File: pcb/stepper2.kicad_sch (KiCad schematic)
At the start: 49 parts, among them J1 DA15_Receptacle_MountingHoles, J10 Conn_01x07_Pin, J2 DA15_Receptacle_MountingHoles, J3 DA15_Receptacle_MountingHoles, J4 DE15_Receptacle_HighDensity, J5 DE15_Receptacle_HighDensity, J6 DE15_Receptacle_HighDensity, J7 Conn_01x04_Pin, J8 Conn_01x05_Pin, J9 Conn_01x06_Pin, SW1 SW_Push, U1 AM26LS32ACN, U2 AM26LS32Ax, U3 AM26LS32ACN, U4 TMC2209_BIGTREETECH, U5 TMC2209_BIGTREETECH, U6 TMC2209_BIGTREETECH

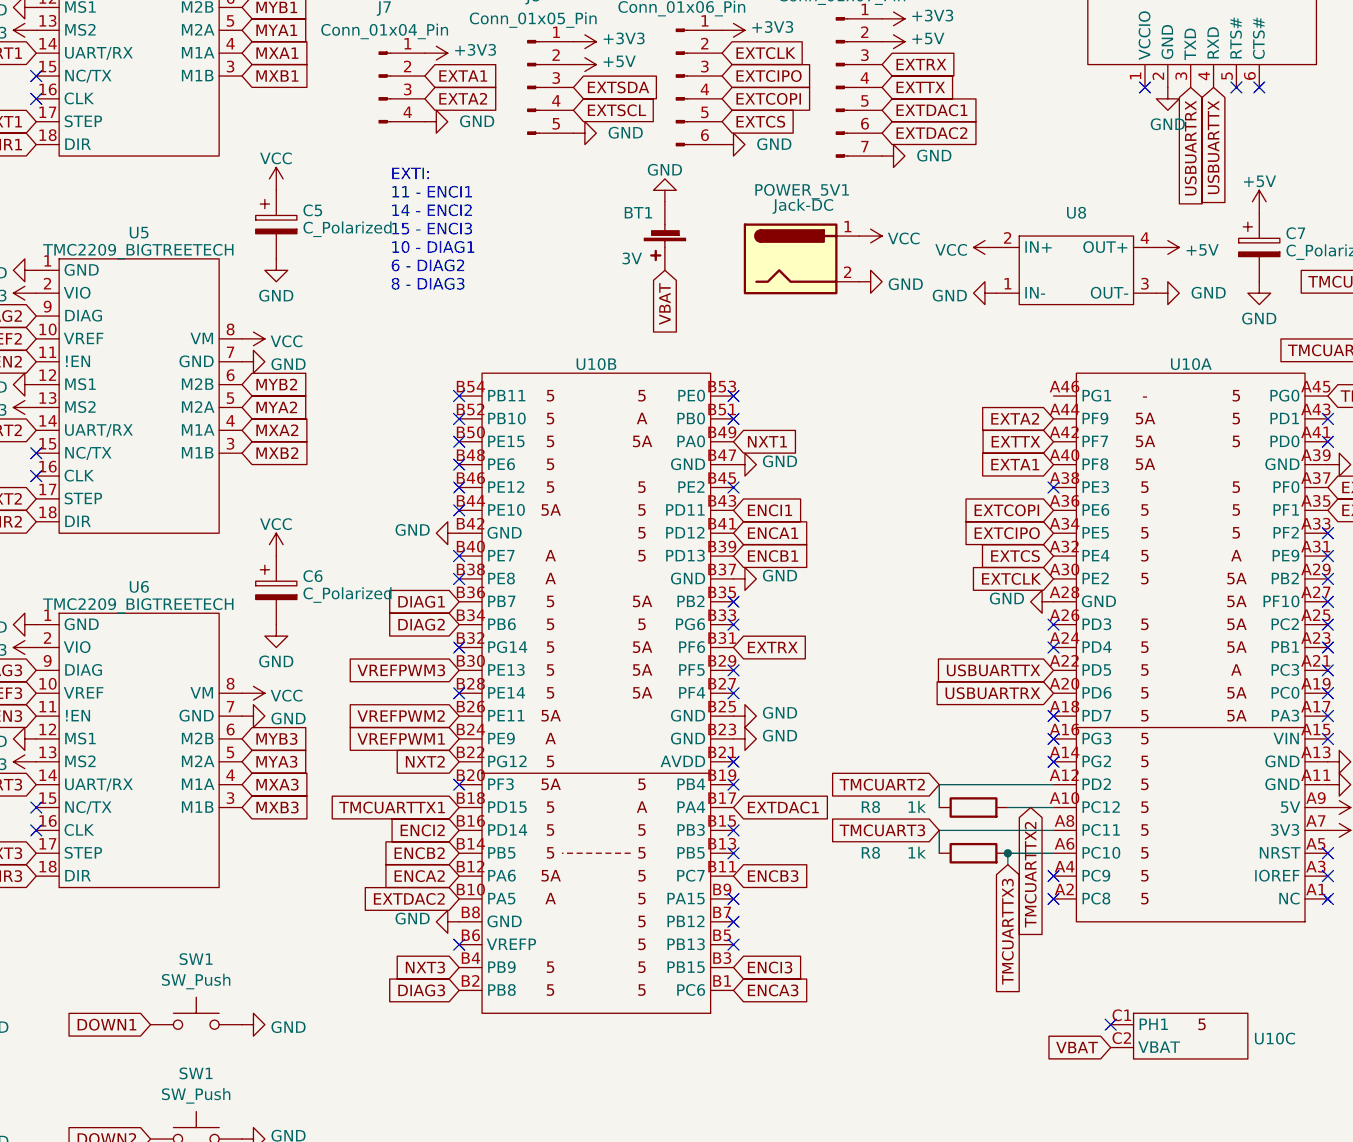
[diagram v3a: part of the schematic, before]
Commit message: Added missing limit switch GPIO and button gpio
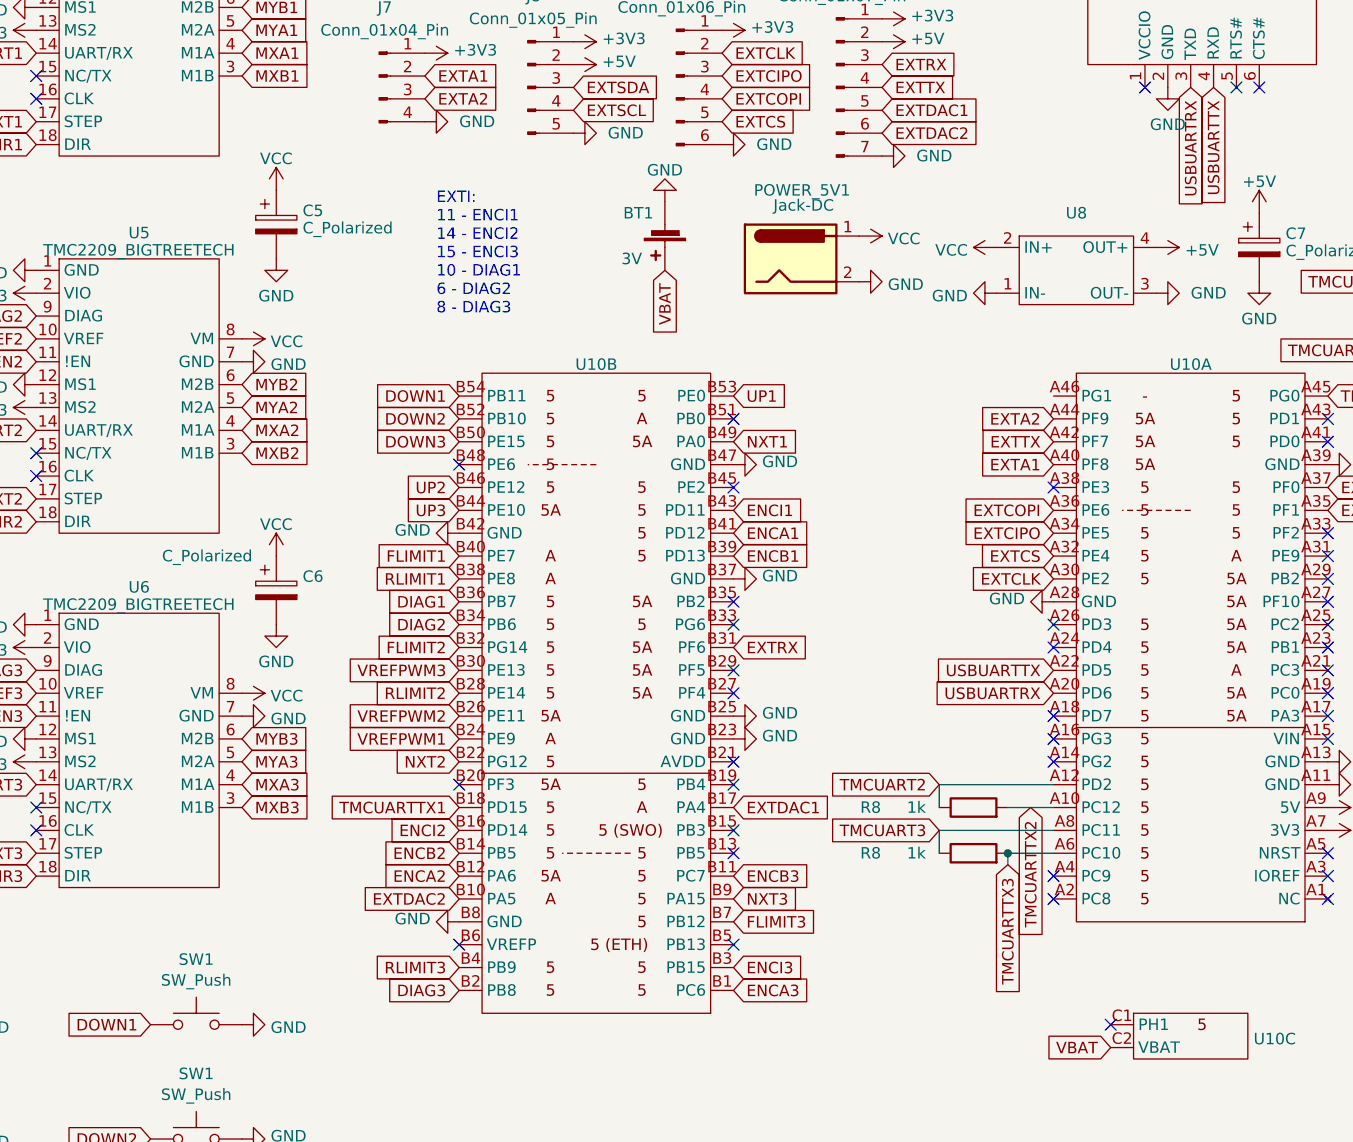
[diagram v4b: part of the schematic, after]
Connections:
- net DOWN1: now also U10.B54 (PB11)
- net DOWN2: now also U10.B52 (PB10)
- net DOWN3: now also U10.B50 (PE15)
- net FLIMIT1: now also U10.B40 (PE7)
- net FLIMIT2: now also U10.B32 (PG14)
- net FLIMIT3: now also U10.B7 (PB12)
- net NXT3: now also U10.B9 (PA15); no longer U10.B4 (PB9)
- net RLIMIT1: now also U10.B38 (PE8)
- net RLIMIT2: now also U10.B28 (PE14)
- net RLIMIT3: now also U10.B4 (PB9)
- net UP1: now also U10.B53 (PE0)
- net UP2: now also U10.B46 (PE12)
- net UP3: now also U10.B44 (PE10)
- no-connect marks 109 -> 97
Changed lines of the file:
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@@
   (no_connect (at 271.78 137.16))
   (no_connect (at 271.78 124.46))
-  (no_connect (at 175.26 88.9))
   (no_connect (at 247.65 156.21))
-  (no_connect (at 175.26 91.44))
-  (no_connect (at 175.26 114.3))
   (no_connect (at 80.01 184.15))
   (no_connect (at 128.27 53.34))
@@
   (no_connect (at 205.74 109.22))
   (no_connect (at 21.59 100.33))
-  (no_connect (at 205.74 137.16))
   (no_connect (at 21.59 33.02))
-  (no_connect (at 205.74 142.24))
   (no_connect (at 271.78 121.92))
   (no_connect (at 270.51 33.02))
   (no_connect (at 128.27 95.25))
-  (no_connect (at 205.74 144.78))
   (no_connect (at 205.74 116.84))
+  (no_connect (at 205.74 129.54))
   (no_connect (at 21.59 147.32))
-  (no_connect (at 205.74 134.62))
+  (no_connect (at 205.74 137.16))
   (no_connect (at 97.79 85.09))
   (no_connect (at 271.78 111.76))
@@
   (no_connect (at 113.03 77.47))
   (no_connect (at 113.03 92.71))
-  (no_connect (at 175.26 99.06))
-  (no_connect (at 175.26 104.14))
   (no_connect (at 241.3 96.52))
   (no_connect (at 21.59 102.87))
+  (no_connect (at 175.26 93.98))
   (no_connect (at 271.78 104.14))
   (no_connect (at 175.26 147.32))
@@
   (no_connect (at 271.78 142.24))
   (no_connect (at 128.27 92.71))
-  (no_connect (at 205.74 86.36))
   (no_connect (at 270.51 30.48))
   (no_connect (at 242.57 30.48))
@@
   (no_connect (at 270.51 38.1))
   (no_connect (at 97.79 58.42))
-  (no_connect (at 175.26 106.68))
   (no_connect (at 241.3 124.46))
   (no_connect (at 271.78 119.38))
@@
   (no_connect (at 270.51 40.64))
   (no_connect (at 97.79 95.25))
-  (no_connect (at 175.26 86.36))
-  (no_connect (at 205.74 147.32))
   (no_connect (at 113.03 55.88))
   (no_connect (at 113.03 116.84))
@@
   (no_connect (at 205.74 96.52))
   (no_connect (at 242.57 33.02))
+  (no_connect (at 205.74 147.32))
   (no_connect (at 271.78 101.6))
   (no_connect (at 21.59 95.25))
@@
   (no_connect (at 241.3 139.7))
   (no_connect (at 205.74 119.38))
-  (no_connect (at 205.74 129.54))
+  (no_connect (at 205.74 134.62))
   (no_connect (at 241.3 111.76))
   (no_connect (at 242.57 35.56))
   (no_connect (at 241.3 127))
-  (no_connect (at 175.26 119.38))
   (no_connect (at 21.59 40.64))
   (no_connect (at 21.59 154.94))
-  (no_connect (at 175.26 93.98))
   (no_connect (at 242.57 40.64))
   (no_connect (at 113.03 132.08))
   (no_connect (at 97.79 124.46))
-  (no_connect (at 175.26 96.52))
   (wire (pts (xy 36.83 45.72) (xy 36.83 48.26))
     (stroke (width 0) (type default))
@@
   )
   (text "EXTI:\n11 - ENCI1\n14 - ENCI2\n15 - ENCI3\n10 - DIAG1\n6 - DIAG2\n8 - DIAG3\n"
-    (at 167.64 74.93 0)
+    (at 172.72 77.47 0)
     (effects (font (size 1.27 1.27)) (justify left bottom))
   )
@@
     )
   )
+  (global_label "UP2" (shape input) (at 175.26 96.52 180) (fields_autoplaced)
+    (effects (font (size 1.27 1.27)) (justify right))
+    (property "Intersheetrefs" "${INTERSHEET_REFS}" (at 168.5442 96.52 0)
+      (effects (font (size 1.27 1.27)) (justify right) hide)
+    )
+  )
   (global_label "EN2" (shape input) (at 128.27 82.55 180) (fields_autoplaced)
     (effects (font (size 1.27 1.27)) (justify right))
@@
     )
   )
+  (global_label "DOWN3" (shape input) (at 175.26 91.44 180) (fields_autoplaced)
+    (effects (font (size 1.27 1.27)) (justify right))
+    (property "Intersheetrefs" "${INTERSHEET_REFS}" (at 165.7623 91.44 0)
+      (effects (font (size 1.27 1.27)) (justify right) hide)
+    )
+  )
   (global_label "ENCA2+" (shape input) (at 21.59 113.03 180) (fields_autoplaced)
     (effects (font (size 1.27 1.27)) (justify right))
@@
     )
   )
+  (global_label "RLIMIT2" (shape input) (at 175.26 119.38 180)
+    (effects (font (size 1.27 1.27)) (justify right))
+    (property "Intersheetrefs" "${INTERSHEET_REFS}" (at 175.26 119.38 0)
+      (effects (font (size 1.27 1.27)) hide)
+    )
+  )
   (global_label "ENCI1+" (shape input) (at 50.8 49.53 180) (fields_autoplaced)
     (effects (font (size 1.27 1.27)) (justify right))
@@
     )
   )
+  (global_label "DOWN2" (shape input) (at 175.26 88.9 180) (fields_autoplaced)
+    (effects (font (size 1.27 1.27)) (justify right))
+    (property "Intersheetrefs" "${INTERSHEET_REFS}" (at 165.7623 88.9 0)
+      (effects (font (size 1.27 1.27)) (justify right) hide)
+    )
+  )
   (global_label "EXTDAC2" (shape input) (at 175.26 142.24 180) (fields_autoplaced)
     (effects (font (size 1.27 1.27)) (justify right))
@@
     )
   )
+  (global_label "UP3" (shape input) (at 175.26 99.06 180) (fields_autoplaced)
+    (effects (font (size 1.27 1.27)) (justify right))
+    (property "Intersheetrefs" "${INTERSHEET_REFS}" (at 168.5442 99.06 0)
+      (effects (font (size 1.27 1.27)) (justify right) hide)
+    )
+  )
   (global_label "ENCB3" (shape input) (at 80.01 156.21 0) (fields_autoplaced)
     (effects (font (size 1.27 1.27)) (justify left))
@@
     )
   )
+  (global_label "FLIMIT2" (shape input) (at 175.26 114.3 180)
+    (effects (font (size 1.27 1.27)) (justify right))
+    (property "Intersheetrefs" "${INTERSHEET_REFS}" (at 175.26 114.3 0)
+      (effects (font (size 1.27 1.27)) hide)
+    )
+  )
   (global_label "ENCI2-" (shape input) (at 36.83 113.03 0) (fields_autoplaced)
     (effects (font (size 1.27 1.27)) (justify left))
@@
     )
   )
+  (global_label "RLIMIT3" (shape input) (at 175.26 149.86 180)
+    (effects (font (size 1.27 1.27)) (justify right))
+    (property "Intersheetrefs" "${INTERSHEET_REFS}" (at 175.26 149.86 0)
+      (effects (font (size 1.27 1.27)) hide)
+    )
+  )
   (global_label "VREF3" (shape input) (at 128.27 119.38 180)
     (effects (font (size 1.27 1.27)) (justify right))
@@
     )
   )
+  (global_label "DOWN1" (shape input) (at 175.26 86.36 180) (fields_autoplaced)
+    (effects (font (size 1.27 1.27)) (justify right))
+    (property "Intersheetrefs" "${INTERSHEET_REFS}" (at 165.7623 86.36 0)
+      (effects (font (size 1.27 1.27)) (justify right) hide)
+    )
+  )
   (global_label "ENCA2-" (shape input) (at 50.8 86.36 180) (fields_autoplaced)
     (effects (font (size 1.27 1.27)) (justify right))
@@
     )
   )
+  (global_label "RLIMIT1" (shape input) (at 175.26 106.68 180)
+    (effects (font (size 1.27 1.27)) (justify right))
+    (property "Intersheetrefs" "${INTERSHEET_REFS}" (at 175.26 106.68 0)
+      (effects (font (size 1.27 1.27)) hide)
+    )
+  )
   (global_label "MXB3" (shape input) (at 151.13 132.08 0) (fields_autoplaced)
     (effects (font (size 1.27 1.27)) (justify left))
@@
     )
   )
+  (global_label "UP1" (shape input) (at 205.74 86.36 0) (fields_autoplaced)
+    (effects (font (size 1.27 1.27)) (justify left))
+    (property "Intersheetrefs" "${INTERSHEET_REFS}" (at 212.4558 86.36 0)
+      (effects (font (size 1.27 1.27)) (justify left) hide)
+    )
+  )
   (global_label "MYA2" (shape input) (at 97.79 92.71 180) (fields_autoplaced)
     (effects (font (size 1.27 1.27)) (justify right))
@@
     )
   )
-  (global_label "NXT3" (shape input) (at 175.26 149.86 180) (fields_autoplaced)
-    (effects (font (size 1.27 1.27)) (justify right))
-    (property "Intersheetrefs" "${INTERSHEET_REFS}" (at 167.6371 149.86 0)
-      (effects (font (size 1.27 1.27)) (justify right) hide)
+  (global_label "NXT3" (shape input) (at 205.74 142.24 0) (fields_autoplaced)
+    (effects (font (size 1.27 1.27)) (justify left))
+    (property "Intersheetrefs" "${INTERSHEET_REFS}" (at 213.3629 142.24 0)
+      (effects (font (size 1.27 1.27)) (justify left) hide)
     )
   )
@@
     )
   )
+  (global_label "FLIMIT1" (shape input) (at 175.26 104.14 180)
+    (effects (font (size 1.27 1.27)) (justify right))
+    (property "Intersheetrefs" "${INTERSHEET_REFS}" (at 175.26 104.14 0)
+      (effects (font (size 1.27 1.27)) hide)
+    )
+  )
   (global_label "TMCUART3" (shape input) (at 228.6 134.62 180) (fields_autoplaced)
     (effects (font (size 1.27 1.27)) (justify right))
@@
     )
   )
+  (global_label "FLIMIT3" (shape input) (at 205.74 144.78 0)
+    (effects (font (size 1.27 1.27)) (justify left))
+    (property "Intersheetrefs" "${INTERSHEET_REFS}" (at 205.74 144.78 0)
+      (effects (font (size 1.27 1.27)) hide)
+    )
+  )
   (global_label "MYA1" (shape input) (at 151.13 45.72 0) (fields_autoplaced)
     (effects (font (size 1.27 1.27)) (justify left))
@@
     )
   )
-  (symbol (lib_id "stepper2:NucleoH723") (at 256.54 114.3 180) (unit 1)
+  (symbol (lib_name "NucleoH723_2") (lib_id "stepper2:NucleoH723") (at 256.54 114.3 180) (unit 1)
     (in_bom yes) (on_board yes) (dnp no) (fields_autoplaced)
     (property "Reference" "U10" (at 256.54 82.8581 0)
@@
     )
   )
-  (symbol (lib_id "stepper2:NucleoH723") (at 190.5 119.38 180) (unit 2)
+  (symbol (lib_name "NucleoH723_1") (lib_id "stepper2:NucleoH723") (at 190.5 119.38 180) (unit 2)
     (in_bom yes) (on_board yes) (dnp no) (fields_autoplaced)
     (property "Reference" "U10" (at 190.5 82.8581 0)
@@
   )
   (symbol (lib_id "Device:C_Polarized") (at 154.94 107.95 0) (unit 1)
-    (in_bom yes) (on_board yes) (dnp no) (fields_autoplaced)
+    (in_bom yes) (on_board yes) (dnp no)
     (property "Reference" "C6" (at 157.861 106.4173 0)
       (effects (font (size 1.27 1.27)) (justify left))
     )
-    (property "Value" "C_Polarized" (at 157.861 108.3383 0)
+    (property "Value" "C_Polarized" (at 142.24 104.14 0)
       (effects (font (size 1.27 1.27)) (justify left))
     )
